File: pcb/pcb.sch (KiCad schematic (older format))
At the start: 127 parts, among them J1 USB_C_Receptacle_USB2.0, J2 AVR-ISP-6, SW1 SW_Push, U1 ATmega32U4-AU, U2 PRTR5V0U2X, Y1 16MHz

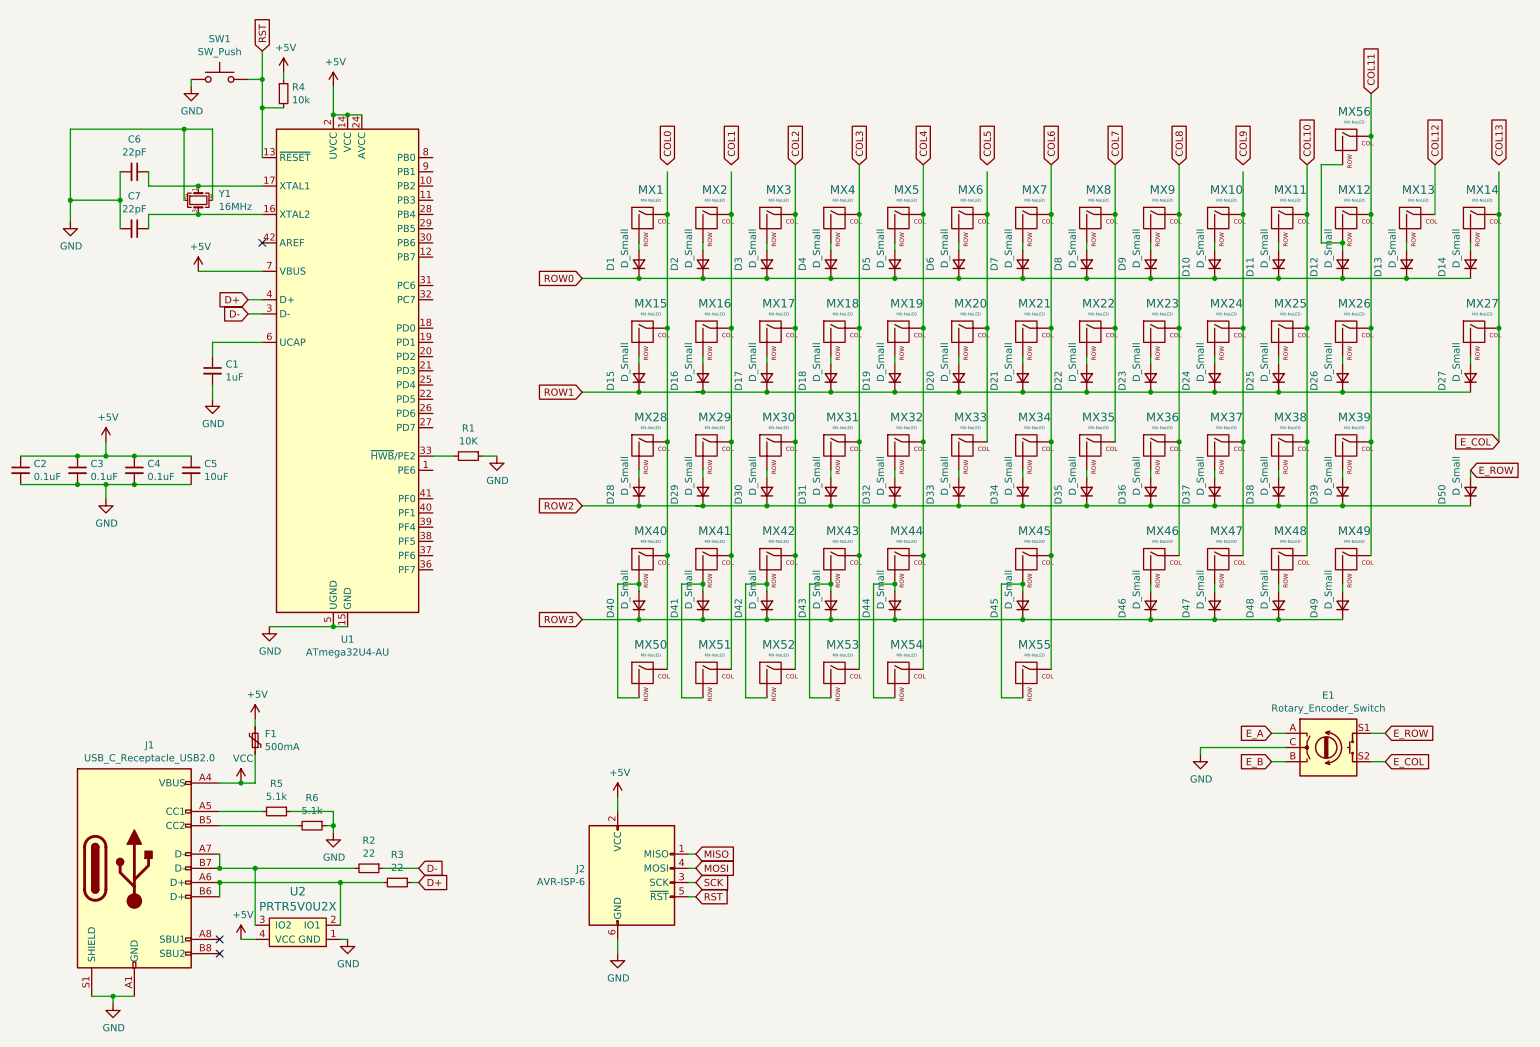
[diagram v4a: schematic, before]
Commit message: route tracks
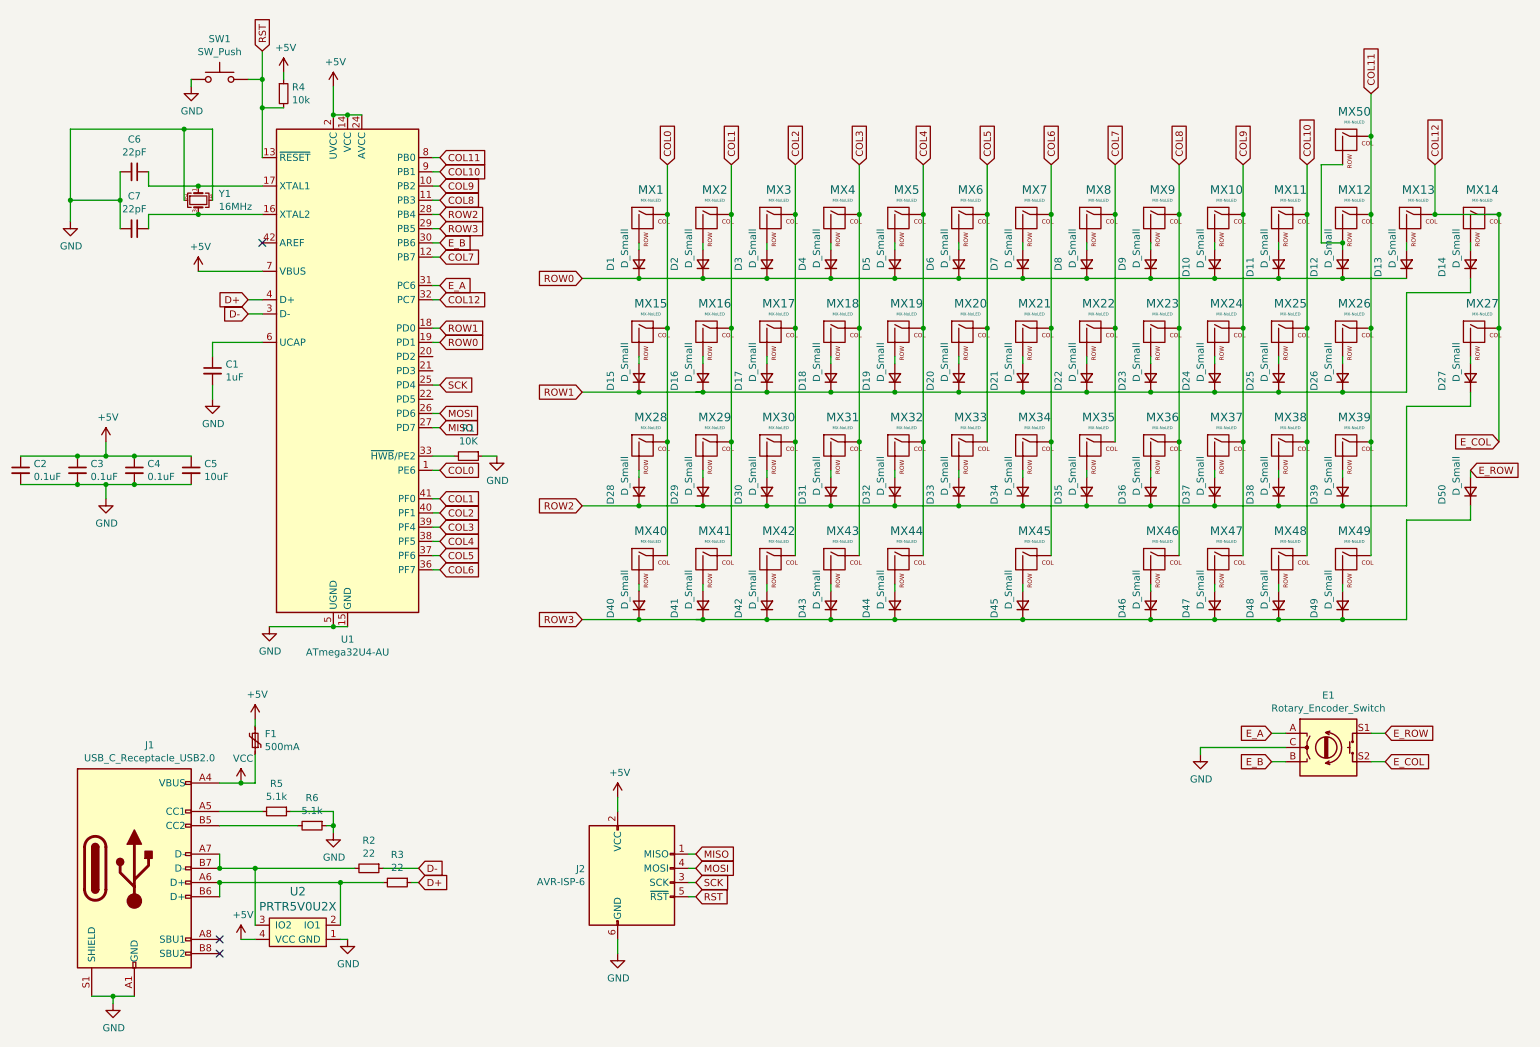
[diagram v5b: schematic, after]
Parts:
- removed MX50, MX51, MX52, MX53, MX55: MX-NoLED, MX_Alps_Hybrid:MX-1.25U, symbol MX_Alps_Hybrid:MX-NoLED
- removed MX54: MX-NoLED, MX_Alps_Hybrid:MX-2.75U, symbol MX_Alps_Hybrid:MX-NoLED
- E1: footprint Rotary_Encoder:RotaryEncoder_Alps_EC11E_Vertical_H20mm -> Rotary_Encoder:RotaryEncoder_Alps_EC11E-Switch_Vertical_H20mm_CircularMountingHoles
- MX1, MX10, MX11, MX12, MX13, MX14, MX16, MX17, MX18, MX19, MX2, MX20, MX21, MX22, MX23, MX24, MX25, MX27, MX29, MX3, MX30, MX31, MX32, MX33, MX34, MX35, MX36, MX37, MX38, MX4, MX40, MX41, MX42, MX43, MX46, MX47, MX48, MX49, MX5, MX6, MX7, MX8, MX9: footprint MX_Alps_Hybrid:MX-1U -> MX_Alps_Hybrid:MX-1U-NoLED
- MX15, MX26: footprint MX_Alps_Hybrid:MX-1.5U -> MX_Alps_Hybrid:MX-1.5U-NoLED
- MX28: footprint MX_Alps_Hybrid:MX-1.75U -> MX_Alps_Hybrid:MX-1.75U-NoLED
- MX39: footprint MX_Alps_Hybrid:MX-1.25U -> MX_Alps_Hybrid:MX-1.25U-NoLED
- MX44: footprint MX_Alps_Hybrid:MX-2.75U -> MX_Alps_Hybrid:MX-2.75U-NoLED
- MX45: footprint MX_Alps_Hybrid:MX-2.25U -> MX_Alps_Hybrid:MX-2.25U-NoLED
- MX50: renamed from MX56; footprint MX_Alps_Hybrid:MX-2U -> MX_Alps_Hybrid:MX-2U-NoLED
- SW1: footprint Button_Switch_SMD:SW_SPST_EVQP7C -> Button_Switch_SMD:SW_SPST_B3U-1000P-B
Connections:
- net labels removed: COL13
- wire segments 263 -> 270

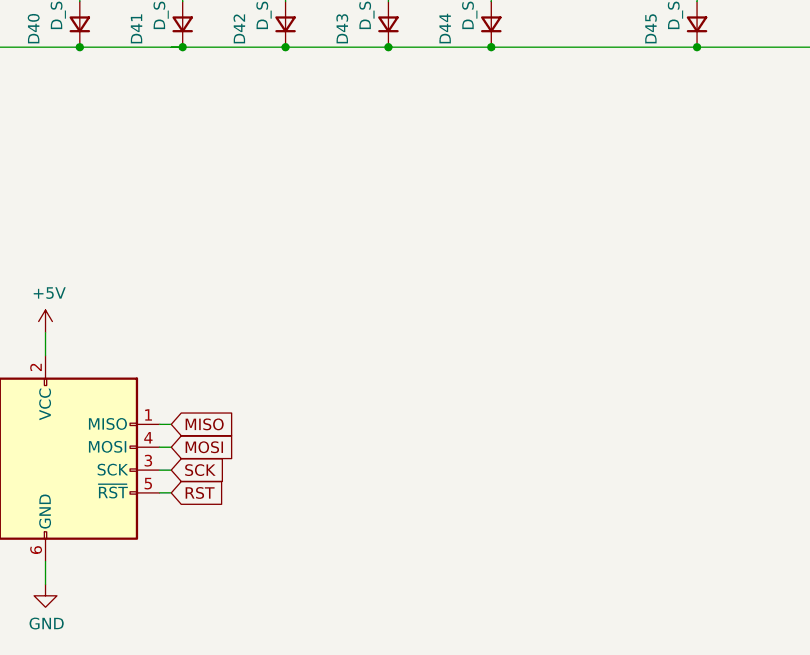
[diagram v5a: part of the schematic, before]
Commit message: correct spacebar placements
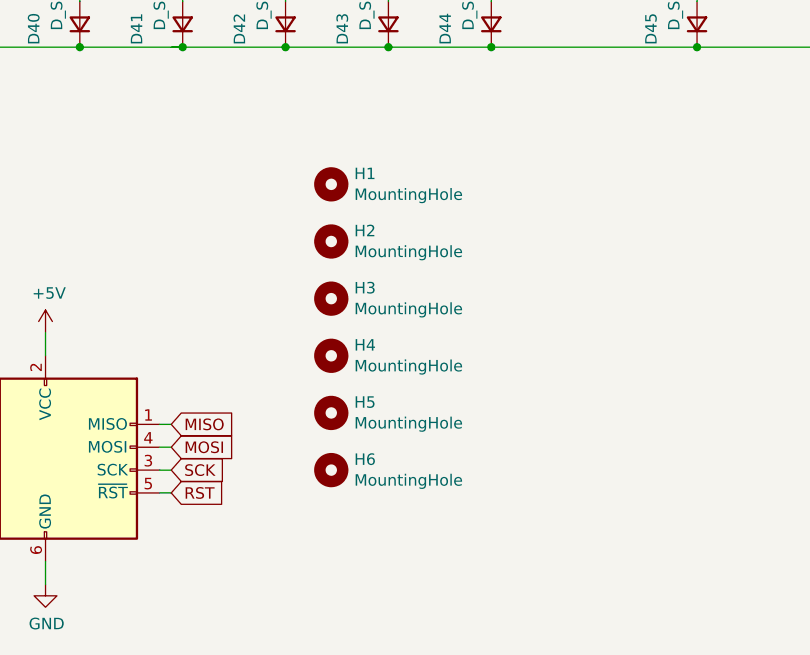
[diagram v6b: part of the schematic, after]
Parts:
- added H1, H2, H3, H4, H5, H6: MountingHole, MountingHole:MountingHole_2.2mm_M2_Pad, symbol Mechanical:MountingHole
- MX44: footprint MX_Alps_Hybrid:MX-2.75U-NoLED -> MX_Alps_Hybrid:MX-2.25U-NoLED
- MX45: footprint MX_Alps_Hybrid:MX-2.25U-NoLED -> MX_Alps_Hybrid:MX-2.75U-NoLED
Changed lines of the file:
@@
 F 0 "MX45" H 7783 4573 60  0000 C CNN
 F 1 "MX-NoLED" H 7783 4499 20  0000 C CNN
-F 2 "MX_Alps_Hybrid:MX-2.25U-NoLED" H 7125 4325 60  0001 C CNN
+F 2 "MX_Alps_Hybrid:MX-2.75U-NoLED" H 7125 4325 60  0001 C CNN
 F 3 "" H 7125 4325 60  0001 C CNN
 	1    7750 4350
@@
 F 0 "MX44" H 6883 4573 60  0000 C CNN
 F 1 "MX-NoLED" H 6883 4499 20  0000 C CNN
-F 2 "MX_Alps_Hybrid:MX-2.75U-NoLED" H 6225 4325 60  0001 C CNN
+F 2 "MX_Alps_Hybrid:MX-2.25U-NoLED" H 6225 4325 60  0001 C CNN
 F 3 "" H 6225 4325 60  0001 C CNN
 	1    6850 4350
@@
 Wire Wire Line
 	5200 1550 5200 1900
+$Comp
+L Mechanical:MountingHole H1
+U 1 1 61D66065
+P 6100 5350
+F 0 "H1" H 6200 5396 50  0000 L CNN
+F 1 "MountingHole" H 6200 5305 50  0000 L CNN
+F 2 "MountingHole:MountingHole_2.2mm_M2_Pad" H 6100 5350 50  0001 C CNN
+F 3 "~" H 6100 5350 50  0001 C CNN
+	1    6100 5350
+	1    0    0    -1
+$EndComp
+$Comp
+L Mechanical:MountingHole H2
+U 1 1 61D67684
+P 6100 5600
+F 0 "H2" H 6200 5646 50  0000 L CNN
+F 1 "MountingHole" H 6200 5555 50  0000 L CNN
+F 2 "MountingHole:MountingHole_2.2mm_M2_Pad" H 6100 5600 50  0001 C CNN
+F 3 "~" H 6100 5600 50  0001 C CNN
+	1    6100 5600
+	1    0    0    -1
+$EndComp
+$Comp
+L Mechanical:MountingHole H3
+U 1 1 61D6788A
+P 6100 5850
+F 0 "H3" H 6200 5896 50  0000 L CNN
+F 1 "MountingHole" H 6200 5805 50  0000 L CNN
+F 2 "MountingHole:MountingHole_2.2mm_M2_Pad" H 6100 5850 50  0001 C CNN
+F 3 "~" H 6100 5850 50  0001 C CNN
+	1    6100 5850
+	1    0    0    -1
+$EndComp
+$Comp
+L Mechanical:MountingHole H4
+U 1 1 61D67B2D
+P 6100 6100
+F 0 "H4" H 6200 6146 50  0000 L CNN
+F 1 "MountingHole" H 6200 6055 50  0000 L CNN
+F 2 "MountingHole:MountingHole_2.2mm_M2_Pad" H 6100 6100 50  0001 C CNN
+F 3 "~" H 6100 6100 50  0001 C CNN
+	1    6100 6100
+	1    0    0    -1
+$EndComp
+$Comp
+L Mechanical:MountingHole H5
+U 1 1 61D67CFA
+P 6100 6350
+F 0 "H5" H 6200 6396 50  0000 L CNN
+F 1 "MountingHole" H 6200 6305 50  0000 L CNN
+F 2 "MountingHole:MountingHole_2.2mm_M2_Pad" H 6100 6350 50  0001 C CNN
+F 3 "~" H 6100 6350 50  0001 C CNN
+	1    6100 6350
+	1    0    0    -1
+$EndComp
+$Comp
+L Mechanical:MountingHole H6
+U 1 1 61D67EAA
+P 6100 6600
+F 0 "H6" H 6200 6646 50  0000 L CNN
+F 1 "MountingHole" H 6200 6555 50  0000 L CNN
+F 2 "MountingHole:MountingHole_2.2mm_M2_Pad" H 6100 6600 50  0001 C CNN
+F 3 "~" H 6100 6600 50  0001 C CNN
+	1    6100 6600
+	1    0    0    -1
+$EndComp
 $EndSCHEMATC

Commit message: 3mm outer spacing
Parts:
- MX44: footprint MX_Alps_Hybrid:MX-2.25U-NoLED -> MX_Alps_Hybrid:MX-2.25U-ReversedStabilizers-NoLED
- MX45: footprint MX_Alps_Hybrid:MX-2.75U-NoLED -> MX_Alps_Hybrid:MX-2.75U-ReversedStabilizers-NoLED
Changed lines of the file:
@@
 	6350 4500 6350 4550
-$Comp
-L MX_Alps_Hybrid:MX-NoLED MX45
-U 1 1 621ACEA1
-P 7750 4350
-F 0 "MX45" H 7783 4573 60  0000 C CNN
-F 1 "MX-NoLED" H 7783 4499 20  0000 C CNN
-F 2 "MX_Alps_Hybrid:MX-2.75U-NoLED" H 7125 4325 60  0001 C CNN
-F 3 "" H 7125 4325 60  0001 C CNN
-	1    7750 4350
-	1    0    0    -1
-$EndComp
 $Comp
 L Device:D_Small D45
@@
 F 0 "MX44" H 6883 4573 60  0000 C CNN
 F 1 "MX-NoLED" H 6883 4499 20  0000 C CNN
-F 2 "MX_Alps_Hybrid:MX-2.25U-NoLED" H 6225 4325 60  0001 C CNN
+F 2 "MX_Alps_Hybrid:MX-2.25U-ReversedStabilizers-NoLED" H 6225 4325 60  0001 C CNN
 F 3 "" H 6225 4325 60  0001 C CNN
 	1    6850 4350
@@
 	1    0    0    -1
 $EndComp
+$Comp
+L MX_Alps_Hybrid:MX-NoLED MX45
+U 1 1 621ACEA1
+P 7750 4350
+F 0 "MX45" H 7783 4573 60  0000 C CNN
+F 1 "MX-NoLED" H 7783 4499 20  0000 C CNN
+F 2 "MX_Alps_Hybrid:MX-2.75U-ReversedStabilizers-NoLED" H 7125 4325 60  0001 C CNN
+F 3 "" H 7125 4325 60  0001 C CNN
+	1    7750 4350
+	1    0    0    -1
+$EndComp
